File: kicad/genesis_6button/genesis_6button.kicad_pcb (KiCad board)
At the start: 2 copper layers, 73.7 x 36.8 mm, 25 parts, among them J1 Conn_02x07_Odd_Even, J2 DB9_Female, J3 Conn_02x03_Odd_Even, U1 74HC257, U2 ATtiny404-SS, U3 74HC257

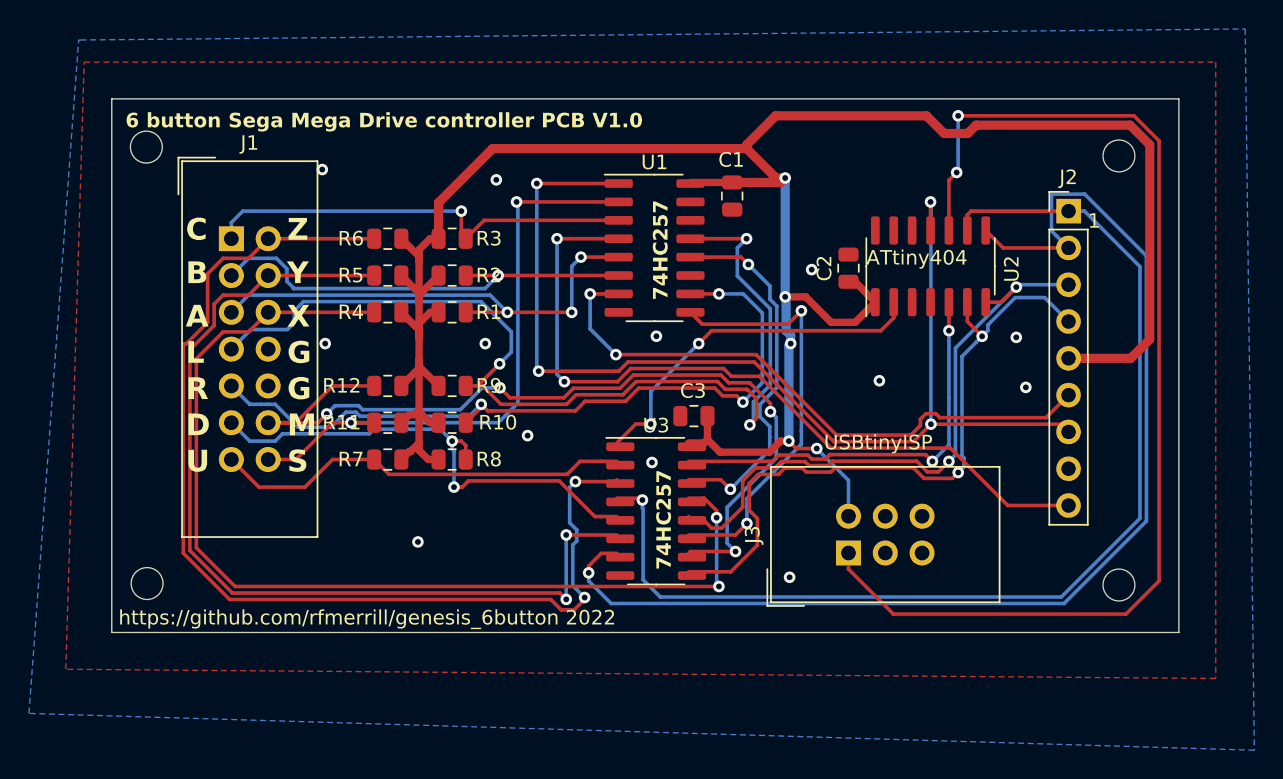
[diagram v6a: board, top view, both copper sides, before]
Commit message: Round off PCB corners
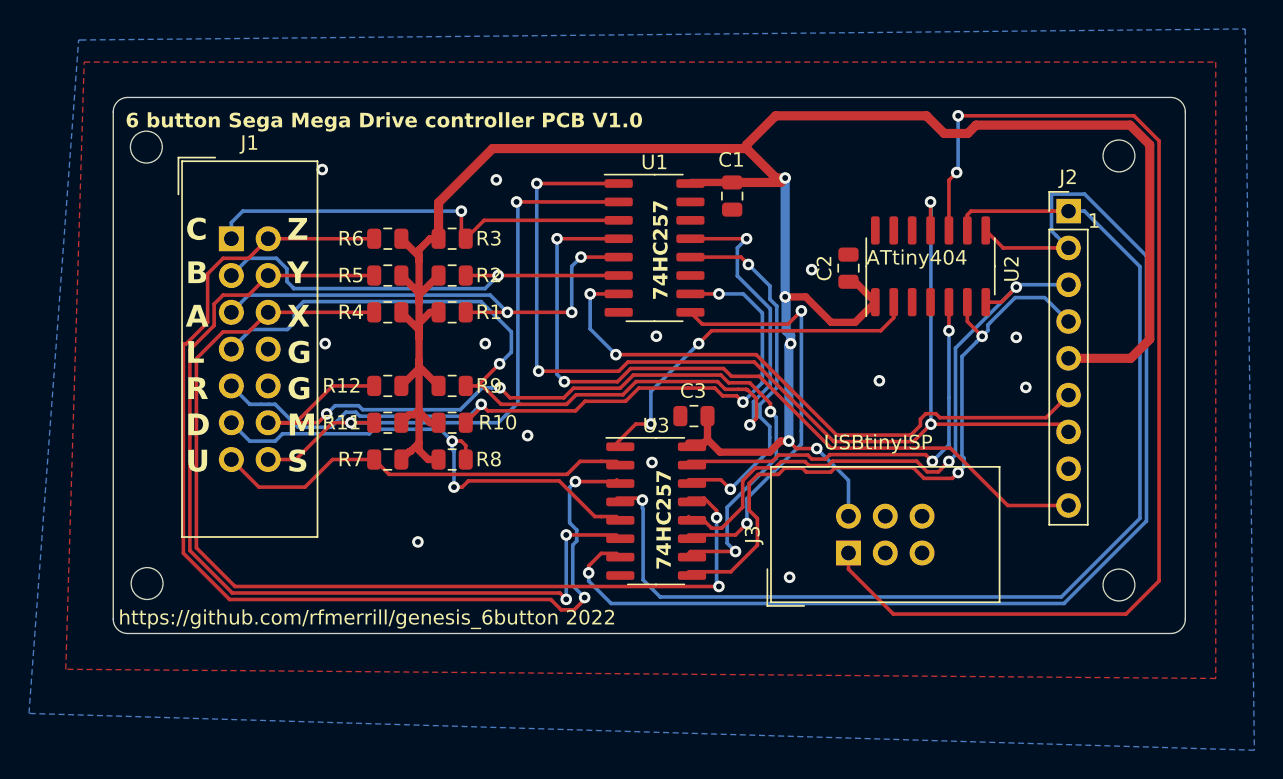
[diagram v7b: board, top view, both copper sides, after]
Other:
- board size 73.7 x 36.8 mm -> 74 x 37 mm
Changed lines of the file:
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@@
 		(embedded_fonts no)
 	)
-	(gr_line
-		(start 88.9 74.93)
-		(end 88.9 38.1)
+	(gr_arc
+		(start 90 75)
+		(mid 89.292893 74.707107)
+		(end 89 74)
 		(stroke
 			(width 0.05)
-			(type solid)
+			(type default)
 		)
 		(layer "Edge.Cuts")
 	)
 	(gr_line
-		(start 162.56 74.93)
-		(end 88.9 74.93)
+		(start 90 38)
+		(end 162 38)
 		(stroke
 			(width 0.05)
-			(type solid)
+			(type default)
+		)
+		(layer "Edge.Cuts")
+	)
+	(gr_arc
+		(start 162 38)
+		(mid 162.707107 38.292893)
+		(end 163 39)
+		(stroke
+			(width 0.05)
+			(type default)
+		)
+		(layer "Edge.Cuts")
+	)
+	(gr_arc
+		(start 89 39)
+		(mid 89.292893 38.292893)
+		(end 90 38)
+		(stroke
+			(width 0.05)
+			(type default)
+		)
+		(layer "Edge.Cuts")
+	)
+	(gr_arc
+		(start 163 74)
+		(mid 162.707107 74.707107)
+		(end 162 75)
+		(stroke
+			(width 0.05)
+			(type default)
 		)
 		(layer "Edge.Cuts")
 	)
 	(gr_line
-		(start 162.56 38.1)
-		(end 162.56 74.93)
+		(start 89 39)
+		(end 89 74)
 		(stroke
 			(width 0.05)
-			(type solid)
+			(type default)
 		)
 		(layer "Edge.Cuts")
 	)
 	(gr_line
-		(start 88.9 38.1)
-		(end 162.56 38.1)
+		(start 90 75)
+		(end 162 75)
 		(stroke
 			(width 0.05)
-			(type solid)
+			(type default)
 		)
 		(layer "Edge.Cuts")
+	)
+	(gr_line
+		(start 163 74)
+		(end 163 39)
+		(stroke
+			(width 0.05)
+			(type default)
+		)
+		(layer "Edge.Cuts")

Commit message: Second revision of silkscreen
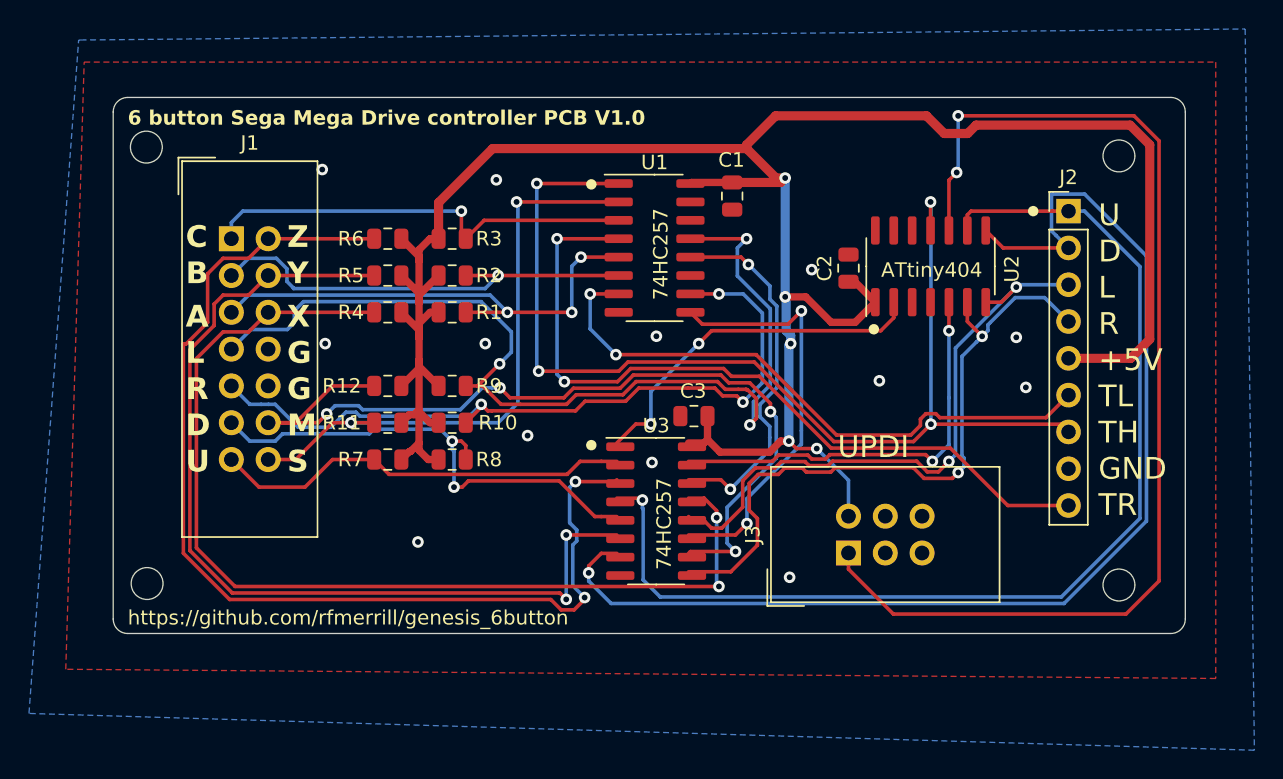
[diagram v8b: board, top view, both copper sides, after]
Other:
- board text added: "+5V"
- board text added: "GND"
- board text added: "TH"
- board text added: "TL"
- board text added: "TR"
- board text added: "UPDI"
- board text added: "https://github.com/rfmerrill/genesis_6button"
- board text removed: "1"
- board text removed: "USBtinyISP"
- board text removed: "https://github.com/rfmerrill/genesis_6button 2022"
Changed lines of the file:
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@@
 		(embedded_fonts no)
+	)
+	(gr_circle
+		(center 152.5 45.847)
+		(end 152.8 45.847)
+		(stroke
+			(width 0.12)
+			(type solid)
+		)
+		(fill yes)
+		(layer "F.SilkS")
+	)
+	(gr_circle
+		(center 141.5 54)
+		(end 141.8 54)
+		(stroke
+			(width 0.12)
+			(type solid)
+		)
+		(fill yes)
+		(layer "F.SilkS")
+	)
+	(gr_circle
+		(center 122 62)
+		(end 122.3 62)
+		(stroke
+			(width 0.12)
+			(type solid)
+		)
+		(fill yes)
+		(layer "F.SilkS")
+	)
+	(gr_circle
+		(center 122 44)
+		(end 122.3 44)
+		(stroke
+			(width 0.12)
+			(type solid)
+		)
+		(fill yes)
+		(layer "F.SilkS")
 	)
 	(gr_arc
@@
 		(layer "Edge.Cuts")
 	)
+	(gr_text "L"
+		(at 157 52 0)
+		(layer "F.SilkS")
+		(effects
+			(font
+				(size 1.5 1.5)
+				(thickness 0.15)
+			)
+			(justify left bottom)
+		)
+	)
 	(gr_text "D"
 		(at 94 61.5 0)
@@
 			(font
 				(size 1.5 1.5)
-				(thickness 0.3)
+				(thickness 0.25)
 				(bold yes)
 			)
@@
 			(font
 				(size 1.5 1.5)
-				(thickness 0.3)
+				(thickness 0.25)
 				(bold yes)
 			)
@@
 	)
 	(gr_text "Z"
-		(at 101 48 0)
-		(layer "F.SilkS")
-		(effects
-			(font
-				(size 1.5 1.5)
-				(thickness 0.3)
+		(at 101 48.5 0)
+		(layer "F.SilkS")
+		(effects
+			(font
+				(size 1.5 1.5)
+				(thickness 0.25)
 				(bold yes)
 			)
@@
 			(font
 				(size 1.5 1.5)
-				(thickness 0.3)
-				(bold yes)
-			)
-			(justify left bottom)
-		)
-	)
-	(gr_text "USBtinyISP"
-		(at 138.049 62.4078 0)
-		(layer "F.SilkS")
-		(effects
-			(font
-				(size 1 1)
+				(thickness 0.25)
+				(bold yes)
+			)
+			(justify left bottom)
+		)
+	)
+	(gr_text "UPDI"
+		(at 139 63 0)
+		(layer "F.SilkS")
+		(effects
+			(font
+				(size 1.5 1.5)
 				(thickness 0.15)
 			)
@@
 			(font
 				(size 1.5 1.5)
-				(thickness 0.3)
+				(thickness 0.25)
 				(bold yes)
 			)
@@
 			(font
 				(size 1.5 1.5)
-				(thickness 0.3)
+				(thickness 0.25)
 				(bold yes)
 			)
@@
 			(font
 				(size 1.5 1.5)
-				(thickness 0.3)
-				(bold yes)
-			)
-			(justify left bottom)
-		)
-	)
-	(gr_text "1"
-		(at 156.27 47.117 0)
-		(layer "F.SilkS")
-		(effects
-			(font
-				(size 1 1)
+				(thickness 0.25)
+				(bold yes)
+			)
+			(justify left bottom)
+		)
+	)
+	(gr_text "+5V"
+		(at 157 57 0)
+		(layer "F.SilkS")
+		(effects
+			(font
+				(size 1.5 1.5)
+				(thickness 0.15)
+			)
+			(justify left bottom)
+		)
+	)
+	(gr_text "GND"
+		(at 157 64.5 0)
+		(layer "F.SilkS")
+		(effects
+			(font
+				(size 1.5 1.5)
+				(thickness 0.15)
+			)
+			(justify left bottom)
+		)
+	)
+	(gr_text "TL"
+		(at 157 59.5 0)
+		(layer "F.SilkS")
+		(effects
+			(font
+				(size 1.5 1.5)
+				(thickness 0.15)
+			)
+			(justify left bottom)
+		)
+	)
+	(gr_text "TR\n"
+		(at 157 67 0)
+		(layer "F.SilkS")
+		(effects
+			(font
+				(size 1.5 1.5)
+				(thickness 0.15)
+			)
+			(justify left bottom)
+		)
+	)
+	(gr_text "TH\n"
+		(at 157 62 0)
+		(layer "F.SilkS")
+		(effects
+			(font
+				(size 1.5 1.5)
 				(thickness 0.15)
 			)
@@
 	)
 	(gr_text "C"
-		(at 94 48 0)
-		(layer "F.SilkS")
-		(effects
-			(font
-				(size 1.5 1.5)
-				(thickness 0.3)
+		(at 94 48.5 0)
+		(layer "F.SilkS")
+		(effects
+			(font
+				(size 1.5 1.5)
+				(thickness 0.25)
 				(bold yes)
 			)
@@
 			(font
 				(size 1.5 1.5)
-				(thickness 0.3)
+				(thickness 0.25)
 				(bold yes)
 			)
@@
 			(font
 				(size 1.5 1.5)
-				(thickness 0.3)
+				(thickness 0.25)
 				(bold yes)
 			)
@@
 			(font
 				(size 1.5 1.5)
-				(thickness 0.3)
-				(bold yes)
-			)
-			(justify left bottom)
-		)
-	)
-	(gr_text "https://github.com/rfmerrill/genesis_6button 2022"
-		(at 89.3572 74.4982 0)
+				(thickness 0.25)
+				(bold yes)
+			)
+			(justify left bottom)
+		)
+	)
+	(gr_text "https://github.com/rfmerrill/genesis_6button"
+		(at 90 74.5 0)
 		(layer "F.SilkS")
 		(effects
 			(font
 				(size 1 1)
+				(thickness 0.15)
+			)
+			(justify left bottom)
+		)
+	)
+	(gr_text "U"
+		(at 157 47 0)
+		(layer "F.SilkS")
+		(effects
+			(font
+				(size 1.5 1.5)
 				(thickness 0.15)
 			)
@@
 			(font
 				(size 1.5 1.5)
-				(thickness 0.3)
+				(thickness 0.25)
 				(bold yes)
 			)
@@
 			(font
 				(size 1 1)
-				(thickness 0.25)
-				(bold yes)
+				(thickness 0.15)
 			)
 			(justify left bottom)
@@
 	)
 	(gr_text "ATtiny404"
-		(at 140.98 49.657 0)
+		(at 142 50.5 0)
 		(layer "F.SilkS")
 		(effects
@@
 			(font
 				(size 1 1)
-				(thickness 0.25)
-				(bold yes)
+				(thickness 0.15)
 			)
 			(justify left bottom)
@@
 			(font
 				(size 1.5 1.5)
-				(thickness 0.3)
+				(thickness 0.25)
 				(bold yes)
 			)
@@
 			(font
 				(size 1.5 1.5)
-				(thickness 0.3)
-				(bold yes)
+				(thickness 0.25)
+				(bold yes)
+			)
+			(justify left bottom)
+		)
+	)
+	(gr_text "D"
+		(at 157 49.5 0)
+		(layer "F.SilkS")
+		(effects
+			(font
+				(size 1.5 1.5)
+				(thickness 0.15)
+			)
+			(justify left bottom)
+		)
+	)
+	(gr_text "R"
+		(at 157 54.5 0)
+		(layer "F.SilkS")
+		(effects
+			(font
+				(size 1.5 1.5)
+				(thickness 0.15)
 			)
 			(justify left bottom)
@@
 	)
 	(gr_text "6 button Sega Mega Drive controller PCB V1.0"
-		(at 89.8398 40.1828 0)
-		(layer "F.SilkS")
-		(effects
+		(at 90 40 0)
+		(layer "F.SilkS")
+		(effects
